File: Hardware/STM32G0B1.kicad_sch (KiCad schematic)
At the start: 25 parts, among them SW1 SW_Push, SW2 SW_Push, SW3 SW_Push, SW4 SW_Push, SW5 SW_Push, Y1 Crystal

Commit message: Replaced the ISOW1044 CAN Transceiver with the ISO1042 + isolated DC-DC and LDO
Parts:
- renumbered C5 to C1, C7 to C2, C6 to C3, C8 to C4, C9 to C5, C1 to C6, C2 to C7, C3 to C8, C4 to C9, R3 to R1, R5 to R2, R4 to R3, R6 to R4, R7 to R5, R1 to R6, R2 to R7, SW3 to SW2, SW2 to SW3
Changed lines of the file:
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@@
 		(on_board yes)
 		(dnp no)
-		(property "Reference" "R5"
+		(property "Reference" "R2"
 			(at 220.98 55.88 90)
 			(effects
@@
 			(project "CANIO-Board"
 				(path "/a11f98b2-3b09-4cf9-8535-19e509fe91b9/4dc55ad2-a09c-41dc-af6c-276c818ee09a"
-					(reference "R5")
+					(reference "R2")
 					(unit 1)
 				)
@@
 		(on_board yes)
 		(dnp no)
-		(property "Reference" "C2"
+		(property "Reference" "C7"
 			(at 36.957 102.87 90)
 			(effects
@@
 			(project "CANIO-Board"
 				(path "/a11f98b2-3b09-4cf9-8535-19e509fe91b9/4dc55ad2-a09c-41dc-af6c-276c818ee09a"
-					(reference "C2")
+					(reference "C7")
 					(unit 1)
 				)
@@
 		(dnp no)
 		(fields_autoplaced yes)
-		(property "Reference" "R1"
+		(property "Reference" "R6"
 			(at 49.53 172.72 90)
 			(effects
@@
 			(project ""
 				(path "/a11f98b2-3b09-4cf9-8535-19e509fe91b9/4dc55ad2-a09c-41dc-af6c-276c818ee09a"
-					(reference "R1")
+					(reference "R6")
 					(unit 1)
 				)
@@
 		(dnp no)
 		(fields_autoplaced yes)
-		(property "Reference" "SW3"
+		(property "Reference" "SW2"
 			(at 214.63 46.9899 90)
 			(effects
@@
 			(project "CANIO-Board"
 				(path "/a11f98b2-3b09-4cf9-8535-19e509fe91b9/4dc55ad2-a09c-41dc-af6c-276c818ee09a"
-					(reference "SW3")
+					(reference "SW2")
 					(unit 1)
 				)
@@
 		(dnp no)
 		(fields_autoplaced yes)
-		(property "Reference" "C8"
+		(property "Reference" "C4"
 			(at 231.14 64.8969 0)
 			(effects
@@
 			(project "CANIO-Board"
 				(path "/a11f98b2-3b09-4cf9-8535-19e509fe91b9/4dc55ad2-a09c-41dc-af6c-276c818ee09a"
-					(reference "C8")
+					(reference "C4")
 					(unit 1)
 				)
@@
 		(dnp no)
 		(fields_autoplaced yes)
-		(property "Reference" "C7"
+		(property "Reference" "C2"
 			(at 231.14 47.1169 0)
 			(effects
@@
 			(project "CANIO-Board"
 				(path "/a11f98b2-3b09-4cf9-8535-19e509fe91b9/4dc55ad2-a09c-41dc-af6c-276c818ee09a"
-					(reference "C7")
+					(reference "C2")
 					(unit 1)
 				)
@@
 		(on_board yes)
 		(dnp no)
-		(property "Reference" "R3"
+		(property "Reference" "R1"
 			(at 158.75 55.88 90)
 			(effects
@@
 			(project "CANIO-Board"
 				(path "/a11f98b2-3b09-4cf9-8535-19e509fe91b9/4dc55ad2-a09c-41dc-af6c-276c818ee09a"
-					(reference "R3")
+					(reference "R1")
 					(unit 1)
 				)
@@
 		(on_board yes)
 		(dnp no)
-		(property "Reference" "C3"
+		(property "Reference" "C8"
 			(at 116.84 184.531 0)
 			(effects
@@
 			(project "CANIO-Board"
 				(path "/a11f98b2-3b09-4cf9-8535-19e509fe91b9/4dc55ad2-a09c-41dc-af6c-276c818ee09a"
-					(reference "C3")
+					(reference "C8")
 					(unit 1)
 				)
@@
 		(dnp no)
 		(fields_autoplaced yes)
-		(property "Reference" "C9"
+		(property "Reference" "C5"
 			(at 231.14 82.6769 0)
 			(effects
@@
 			(project "CANIO-Board"
 				(path "/a11f98b2-3b09-4cf9-8535-19e509fe91b9/4dc55ad2-a09c-41dc-af6c-276c818ee09a"
-					(reference "C9")
+					(reference "C5")
 					(unit 1)
 				)
@@
 		(dnp no)
 		(fields_autoplaced yes)
-		(property "Reference" "C5"
+		(property "Reference" "C1"
 			(at 168.91 47.1169 0)
 			(effects
@@
 			(project ""
 				(path "/a11f98b2-3b09-4cf9-8535-19e509fe91b9/4dc55ad2-a09c-41dc-af6c-276c818ee09a"
-					(reference "C5")
+					(reference "C1")
 					(unit 1)
 				)
@@
 		(on_board yes)
 		(dnp no)
-		(property "Reference" "R7"
+		(property "Reference" "R5"
 			(at 220.98 91.44 90)
 			(effects
@@
 			(project "CANIO-Board"
 				(path "/a11f98b2-3b09-4cf9-8535-19e509fe91b9/4dc55ad2-a09c-41dc-af6c-276c818ee09a"
-					(reference "R7")
+					(reference "R5")
 					(unit 1)
 				)
@@
 		(dnp no)
 		(fields_autoplaced yes)
-		(property "Reference" "C6"
+		(property "Reference" "C3"
 			(at 168.91 64.8969 0)
 			(effects
@@
 			(project "CANIO-Board"
 				(path "/a11f98b2-3b09-4cf9-8535-19e509fe91b9/4dc55ad2-a09c-41dc-af6c-276c818ee09a"
-					(reference "C6")
+					(reference "C3")
 					(unit 1)
 				)
@@
 		(on_board yes)
 		(dnp no)
-		(property "Reference" "C4"
+		(property "Reference" "C9"
 			(at 139.7 184.531 0)
 			(effects
@@
 			(project "CANIO-Board"
 				(path "/a11f98b2-3b09-4cf9-8535-19e509fe91b9/4dc55ad2-a09c-41dc-af6c-276c818ee09a"
-					(reference "C4")
+					(reference "C9")
 					(unit 1)
 				)
@@
 		(on_board yes)
 		(dnp no)
-		(property "Reference" "R4"
+		(property "Reference" "R3"
 			(at 158.75 73.66 90)
 			(effects
@@
 			(project "CANIO-Board"
 				(path "/a11f98b2-3b09-4cf9-8535-19e509fe91b9/4dc55ad2-a09c-41dc-af6c-276c818ee09a"
-					(reference "R4")
+					(reference "R3")
 					(unit 1)
 				)
@@
 		(on_board yes)
 		(dnp no)
-		(property "Reference" "R2"
+		(property "Reference" "R7"
 			(at 49.53 188.214 90)
 			(effects
@@
 			(project "CANIO-Board"
 				(path "/a11f98b2-3b09-4cf9-8535-19e509fe91b9/4dc55ad2-a09c-41dc-af6c-276c818ee09a"
-					(reference "R2")
+					(reference "R7")
 					(unit 1)
 				)
@@
 		(dnp no)
 		(fields_autoplaced yes)
-		(property "Reference" "SW2"
+		(property "Reference" "SW3"
 			(at 152.4 64.7699 90)
 			(effects
@@
 			(project "CANIO-Board"
 				(path "/a11f98b2-3b09-4cf9-8535-19e509fe91b9/4dc55ad2-a09c-41dc-af6c-276c818ee09a"
-					(reference "SW2")
+					(reference "SW3")
 					(unit 1)
 				)
@@
 		(on_board yes)
 		(dnp no)
-		(property "Reference" "C1"
+		(property "Reference" "C6"
 			(at 36.957 86.36 90)
 			(effects
@@
 			(project "CANIO-Board"
 				(path "/a11f98b2-3b09-4cf9-8535-19e509fe91b9/4dc55ad2-a09c-41dc-af6c-276c818ee09a"
-					(reference "C1")
+					(reference "C6")
 					(unit 1)
 				)
@@
 		(on_board yes)
 		(dnp no)
-		(property "Reference" "R6"
+		(property "Reference" "R4"
 			(at 220.98 73.66 90)
 			(effects
@@
 			(project "CANIO-Board"
 				(path "/a11f98b2-3b09-4cf9-8535-19e509fe91b9/4dc55ad2-a09c-41dc-af6c-276c818ee09a"
-					(reference "R6")
-					(unit 1)
-				)
+					(reference "R4")
+					(unit 1)
+				)

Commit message: Updated the USB-C connector from 14 pin to 16 pin
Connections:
- net CAN_IN: no longer names the net of MCU1.20 (PC6)
- net CAN_STB: no longer names the net of MCU1.26 (PA15)
- no-connect marks 1 -> 3
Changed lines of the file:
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@@
+	)
+	(no_connect
+		(at 30.48 52.07)
 	)
 	(no_connect
 		(at 30.48 67.31)
 	)
+	(no_connect
+		(at 104.14 85.09)
+	)
 	(bus_entry
 		(at 73.66 147.32)
@@
 		(at 30.48 80.01)
 		(size -2.54 -2.54)
-		(stroke
-			(width 0)
-			(type default)
-		)
-	)
-	(bus_entry
-		(at 39.37 162.56)
-		(size -2.54 -2.54)
-		(stroke
-			(width 0)
-			(type default)
-		)
-	)
-	(bus_entry
-		(at 104.14 85.09)
-		(size 2.54 -2.54)
 		(stroke
 			(width 0)
@@
 	)
 	(bus_entry
-		(at 39.37 165.1)
-		(size -2.54 -2.54)
-		(stroke
-			(width 0)
-			(type default)
-		)
-	)
-	(bus_entry
 		(at 104.14 59.69)
 		(size 2.54 -2.54)
@@
 	)
 	(bus_entry
-		(at 30.48 52.07)
-		(size -2.54 -2.54)
-		(stroke
-			(width 0)
-			(type default)
-		)
-	)
-	(bus_entry
 		(at 73.66 137.16)
 		(size -2.54 -2.54)
@@
 		)
 	)
-	(bus
-		(pts
-			(xy 27.94 44.45) (xy 27.94 49.53)
-		)
-		(stroke
-			(width 0)
-			(type default)
-		)
-	)
 	(wire
 		(pts
@@
 		(pts
 			(xy 36.83 129.54) (xy 36.83 127)
-		)
-		(stroke
-			(width 0)
-			(type default)
-		)
-	)
-	(wire
-		(pts
-			(xy 39.37 162.56) (xy 50.8 162.56)
 		)
 		(stroke
@@
 		)
 	)
-	(bus
-		(pts
-			(xy 36.83 157.48) (xy 36.83 160.02)
-		)
-		(stroke
-			(width 0)
-			(type default)
-		)
-	)
 	(wire
 		(pts
@@
 		)
 	)
-	(bus
-		(pts
-			(xy 106.68 80.01) (xy 106.68 82.55)
-		)
-		(stroke
-			(width 0)
-			(type default)
-		)
-	)
 	(wire
 		(pts
@@
 	(bus
 		(pts
-			(xy 27.94 49.53) (xy 27.94 59.69)
+			(xy 27.94 44.45) (xy 27.94 59.69)
 		)
 		(stroke
@@
 		(pts
 			(xy 30.48 69.85) (xy 41.91 69.85)
-		)
-		(stroke
-			(width 0)
-			(type default)
-		)
-	)
-	(wire
-		(pts
-			(xy 39.37 165.1) (xy 50.8 165.1)
-		)
-		(stroke
-			(width 0)
-			(type default)
-		)
-	)
-	(bus
-		(pts
-			(xy 36.83 160.02) (xy 36.83 162.56)
 		)
 		(stroke
@@
 		)
 	)
-	(label "CAN_STB"
-		(at 50.8 162.56 180)
-		(effects
-			(font
-				(size 1.27 1.27)
-			)
-			(justify right bottom)
-		)
-	)
 	(label "GPIO2"
 		(at 104.14 54.61 180)
@@
 		)
 	)
-	(label "CAN_IN"
-		(at 30.48 52.07 0)
-		(effects
-			(font
-				(size 1.27 1.27)
-			)
-			(justify left bottom)
-		)
-	)
-	(label "CAN_STB"
-		(at 104.14 85.09 180)
-		(effects
-			(font
-				(size 1.27 1.27)
-			)
-			(justify right bottom)
-		)
-	)
 	(label "NRST"
 		(at 85.09 147.32 180)
@@
 		)
 	)
-	(label "CAN_IN"
-		(at 50.8 165.1 180)
-		(effects
-			(font
-				(size 1.27 1.27)
-			)
-			(justify right bottom)
-		)
-	)

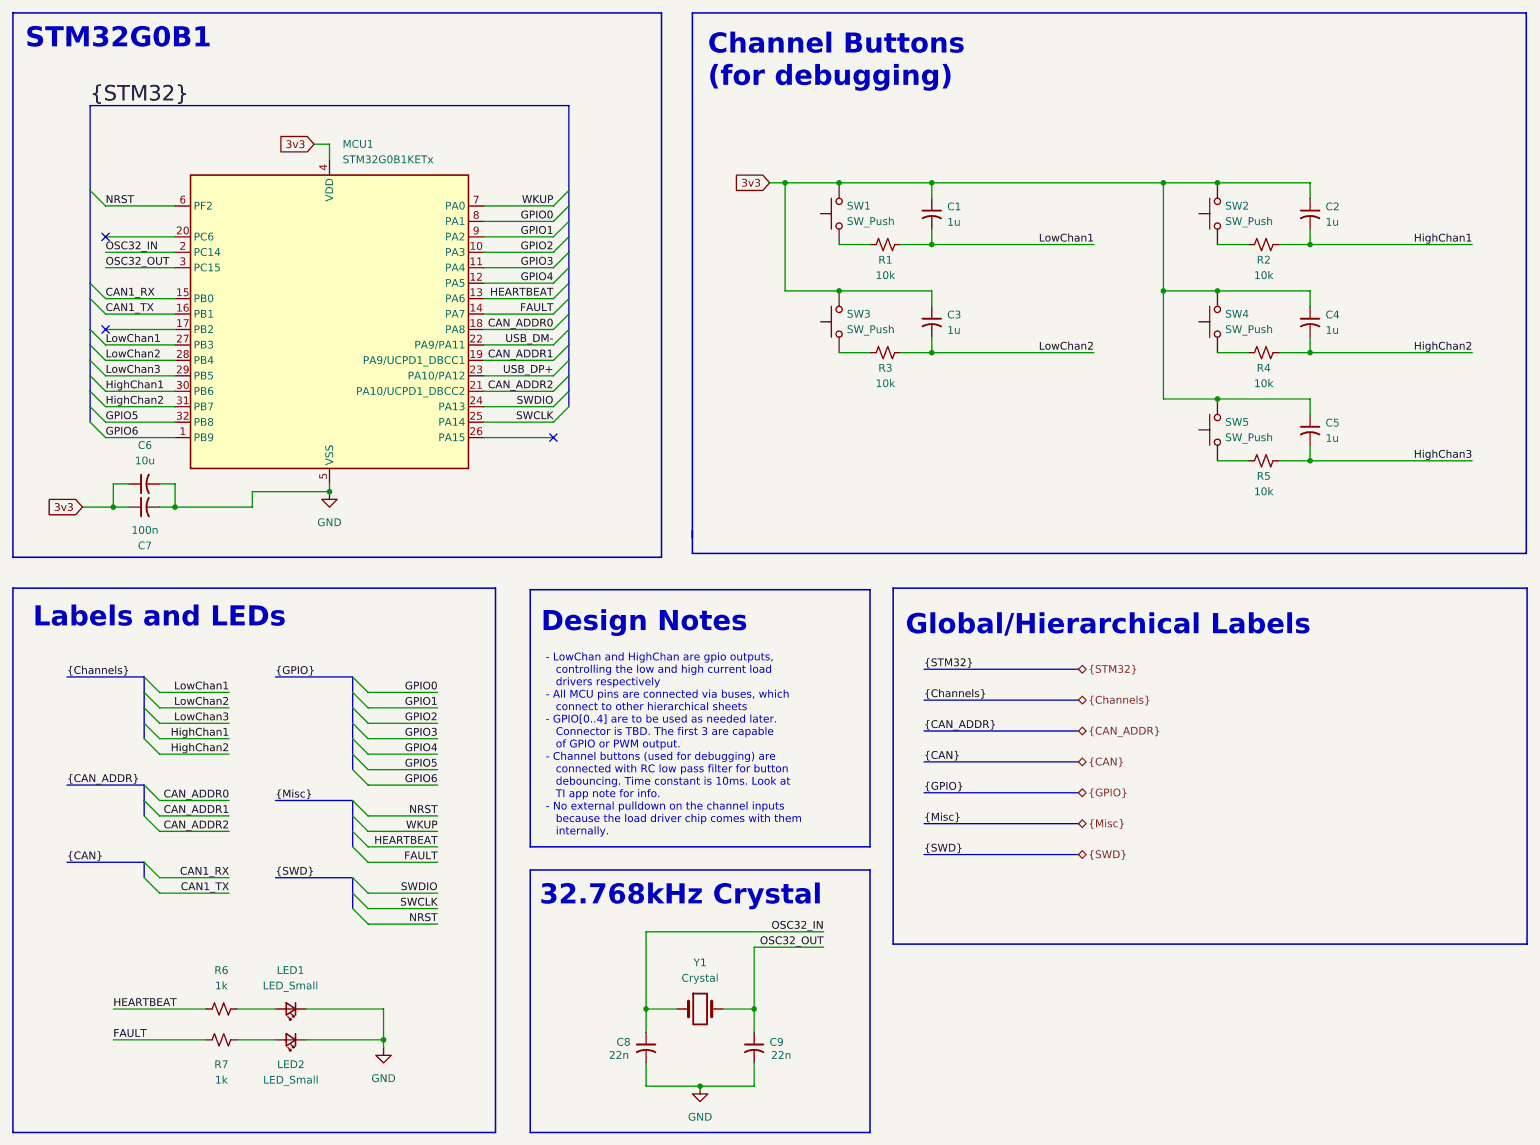
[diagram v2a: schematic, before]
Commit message: Replaced G0B1KET6 with KET6N in schematic
- Updated the schematic with new symbol and pinout.
- Updated the rest of the schematic with all resulting changes
	- This includes the 8 output channels, 7 GPIOs, and slightly
	  different WAGO connector configuration.
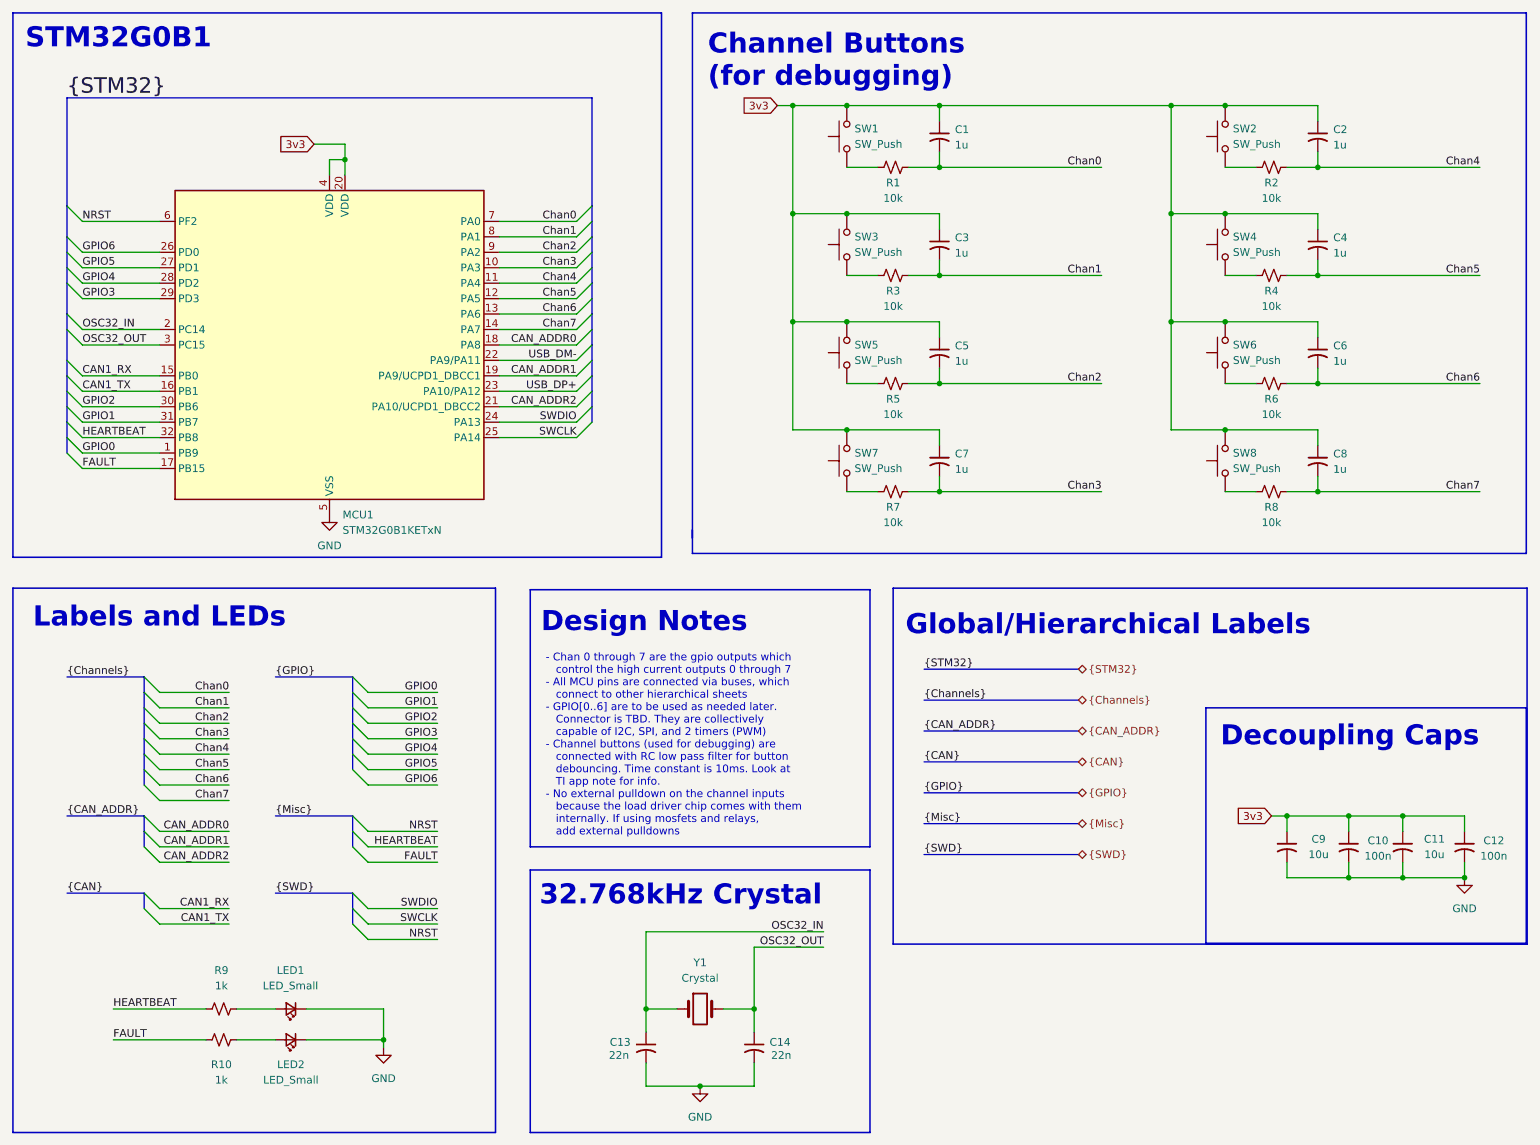
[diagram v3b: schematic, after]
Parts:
- removed MCU1: STM32G0B1KETx, Package_QFP:LQFP-32_7x7mm_P0.8mm, symbol MCU_ST_STM32G0:STM32G0B1KETx
- added C11: 10u, Capacitor_SMD:C_0603_1608Metric_Pad1.08x0.95mm_HandSolder, symbol Device:C_Small_US
- added C12: 100n, Capacitor_SMD:C_0603_1608Metric_Pad1.08x0.95mm_HandSolder, symbol Device:C_Small_US
- added C5, C7, C8: 1u, Capacitor_SMD:C_0603_1608Metric_Pad1.08x0.95mm_HandSolder, symbol Device:C_Small_US
- added MCU1: STM32G0B1KETxN, Package_QFP:LQFP-32_7x7mm_P0.8mm, symbol MCU_ST_STM32G0:STM32G0B1KETxN
- added R5, R7, R8: 10k, Resistor_SMD:R_0603_1608Metric_Pad0.98x0.95mm_HandSolder, symbol Device:R_Small_US
- added SW5, SW7, SW8: SW_Push, Button_Switch_SMD:SW_Push_1P1T_NO_CK_KSC7xxJ, symbol Switch:SW_Push
- renumbered C7 to C10, C8 to C13, C9 to C14, C5 to C6, C6 to C9, R7 to R10, R5 to R6, R6 to R9, SW5 to SW6
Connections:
- net 3v3: now also C11.1, C12.1, C5.1, C7.1, C8.1, MCU1.20 (VDD), MCU1.4 (VDD), SW5.2, SW7.2, SW8.2
- net CAN1_RX: now also MCU1.15 (PB0)
- net CAN1_TX: now also MCU1.16 (PB1)
- net CAN_ADDR0: now also MCU1.18 (PA8)
- net CAN_ADDR1: now also MCU1.19 (PA9/UCPD1_DBCC1)
- net CAN_ADDR2: now also MCU1.21 (PA10/UCPD1_DBCC2)
- net FAULT: now also MCU1.17 (PB15)
- net GND: now also C11.2, C12.2, MCU1.5 (VSS)
- net GPIO0: now also MCU1.1 (PB9)
- net GPIO1: now also MCU1.31 (PB7)
- net GPIO2: now also MCU1.30 (PB6)
- net GPIO3: now also MCU1.29 (PD3)
- net GPIO4: now also MCU1.28 (PD2)
- net GPIO5: now also MCU1.27 (PD1)
- net GPIO6: now also MCU1.26 (PD0)
- net HEARTBEAT: now also MCU1.32 (PB8)
- net NRST: now also MCU1.6 (PF2)
- net OSC32_IN: now also MCU1.2 (PC14)
- net OSC32_OUT: now also MCU1.3 (PC15)
- net SWCLK: now also MCU1.25 (PA14)
- net SWDIO: now also MCU1.24 (PA13)
- net USB_DM-: now also MCU1.22 (PA9/PA11)
- net USB_DP+: now also MCU1.23 (PA10/PA12)
- net HighChan1 renamed Chan4
- net Chan4: now also MCU1.11 (PA4)
- net HighChan2 renamed Chan5
- net Chan5: now also MCU1.12 (PA5)
- net HighChan3 renamed Chan6
- net Chan6: now also MCU1.13 (PA6)
- net LowChan1 renamed Chan0
- net Chan0: now also MCU1.7 (PA0)
- net LowChan2 renamed Chan1
- net Chan1: now also MCU1.8 (PA1)
- new net: R5.2, SW5.1
- new net: R7.2, SW7.1
- new net: R8.2, SW8.1
- new net Chan2: C5.2, MCU1.9 (PA2), R5.1
- new net Chan3: C7.2, MCU1.10 (PA3), R7.1
- new net Chan7: C8.2, MCU1.14 (PA7), R8.1
- no-connect marks 3 -> 0
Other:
- note added: "- Chan 0 through 7 are the gpio outputs which control the high current outputs 0 through 7 - All MCU pins are connected via buses, which connect to other hierarchical sheets - GPIO[0..6] are to be used as needed later. Connector is TBD. They are collectively capable of I2C, SPI, and 2 timers (PWM) - Channel buttons (used for debugging) are connected with RC low pass filter for button debouncing. 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"
- note added: "Decoupling Caps"
- note removed: "- LowChan and HighChan are gpio outputs, controlling the low and high current load drivers respectively - All MCU pins are connected via buses, which connect to other hierarchical sheets - GPIO[0..4] are to be used as needed later. Connector is TBD. The first 3 are capable of GPIO or PWM output. - Channel buttons (used for debugging) are connected with RC low pass filter for button debouncing. Ti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"
- moved on the sheet: C1, C10, C2, C3, C4, C6, C9, R1, R2, R3, R4, R6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

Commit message: Finished the board
- Board layout and routing is finished. Need to fix ~30 ERC errors and
  add thorough notes throughout, but otherwise that's it.
- Once ERC errors are resolved, will post BOM and Gerbers as a release.
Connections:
- net Chan1: now also C2.2, R2.1; no longer C3.2, R3.1
- net Chan2: now also C3.2, R3.1; no longer C5.2, R5.1
- net Chan3: now also C4.2, R4.1; no longer C7.2, R7.1
- net Chan4: now also C5.2, R5.1; no longer C2.2, R2.1
- net Chan5: now also C6.2, R6.1; no longer C4.2, R4.1
- net Chan6: now also C7.2, R7.1; no longer C6.2, R6.1
- net USB_DM- renamed USB_DF-
- net USB_DP+ renamed USB_DF+
